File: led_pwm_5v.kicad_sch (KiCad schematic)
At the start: 4 parts, among them Q11 BC846, Q12 AO3423

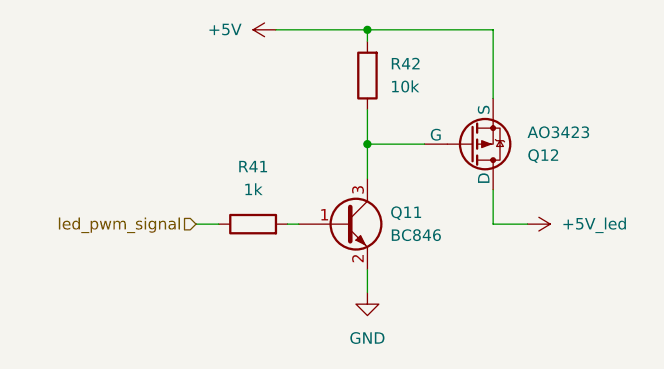
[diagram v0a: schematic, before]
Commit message: Schematic sites change
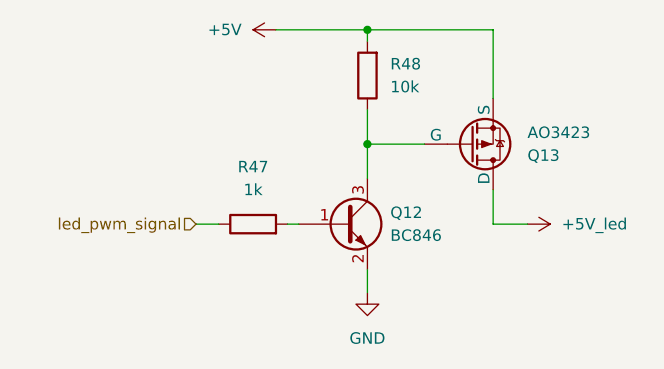
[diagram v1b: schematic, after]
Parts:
- renumbered Q11 to Q12, Q12 to Q13, R41 to R47, R42 to R48
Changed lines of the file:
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@@
 		(dnp no)
 		(fields_autoplaced yes)
-		(property "Reference" "R42"
+		(property "Reference" "R48"
 			(at 95.25 41.9099 0)
 			(effects
@@
 			(project "rpm_meter"
 				(path "/c95b12ac-441d-4f7a-bd6a-c2e5d81eb286/78a0b38c-312f-4578-a70f-0ba40d57e033"
-					(reference "R42")
+					(reference "R48")
 					(unit 1)
 				)
@@
 		(dnp no)
 		(fields_autoplaced yes)
-		(property "Reference" "Q11"
+		(property "Reference" "Q12"
 			(at 95.25 58.4199 0)
 			(effects
@@
 			(project ""
 				(path "/c95b12ac-441d-4f7a-bd6a-c2e5d81eb286/78a0b38c-312f-4578-a70f-0ba40d57e033"
-					(reference "Q11")
+					(reference "Q12")
 					(unit 1)
 				)
@@
 		(on_board yes)
 		(dnp no)
-		(property "Reference" "Q12"
+		(property "Reference" "Q13"
 			(at 110.49 52.0701 0)
 			(effects
@@
 			(project ""
 				(path "/c95b12ac-441d-4f7a-bd6a-c2e5d81eb286/78a0b38c-312f-4578-a70f-0ba40d57e033"
-					(reference "Q12")
+					(reference "Q13")
 					(unit 1)
 				)
@@
 		(dnp no)
 		(fields_autoplaced yes)
-		(property "Reference" "#PWR021"
+		(property "Reference" "#PWR029"
 			(at 92.71 73.66 0)
 			(effects
@@
 			(project ""
 				(path "/c95b12ac-441d-4f7a-bd6a-c2e5d81eb286/78a0b38c-312f-4578-a70f-0ba40d57e033"
-					(reference "#PWR021")
+					(reference "#PWR029")
 					(unit 1)
 				)
@@
 		(dnp no)
 		(fields_autoplaced yes)
-		(property "Reference" "#PWR023"
+		(property "Reference" "#PWR028"
 			(at 86.36 38.1 0)
 			(effects
@@
 			(project ""
 				(path "/c95b12ac-441d-4f7a-bd6a-c2e5d81eb286/78a0b38c-312f-4578-a70f-0ba40d57e033"
-					(reference "#PWR023")
+					(reference "#PWR028")
 					(unit 1)
 				)
@@
 		(dnp no)
 		(fields_autoplaced yes)
-		(property "Reference" "#PWR022"
+		(property "Reference" "#PWR030"
 			(at 106.68 59.69 0)
 			(effects
@@
 			(project "rpm_meter"
 				(path "/c95b12ac-441d-4f7a-bd6a-c2e5d81eb286/78a0b38c-312f-4578-a70f-0ba40d57e033"
-					(reference "#PWR022")
+					(reference "#PWR030")
 					(unit 1)
 				)
@@
 		(dnp no)
 		(fields_autoplaced yes)
-		(property "Reference" "R41"
+		(property "Reference" "R47"
 			(at 80.01 53.34 90)
 			(effects
@@
 			(project ""
 				(path "/c95b12ac-441d-4f7a-bd6a-c2e5d81eb286/78a0b38c-312f-4578-a70f-0ba40d57e033"
-					(reference "R41")
-					(unit 1)
-				)
+					(reference "R47")
+					(unit 1)
+				)

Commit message: New template
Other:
- company: (none) -> STAPsystem
- title: (none) -> RPM meter LED
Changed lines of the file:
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@@
 	(generator_version "8.0")
 	(paper "A5")
+	(title_block
+		(title "RPM meter LED")
+		(date "2024-11-26")
+		(rev "v1.0")
+		(company "STAPsystem")
+	)
 	(junction
 		(at 92.71 50.8)
